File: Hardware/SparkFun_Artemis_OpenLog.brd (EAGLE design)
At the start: 30.5 x 30.5 mm, 112 parts, among them J11 Qwiic, J14 CORTEX_JTAG, J17 MICRO-SD, Q1 20V/0.2A/8MHz/1.2Ω/1Vth, Q10 20V/0.2A/8MHz/1.2Ω/1Vth, Q3 20V/0.2A/8MHz/1.2Ω/1Vth, Q7 20V/0.2A/8MHz/1.2Ω/1Vth, Q9 20V/0.2A/8MHz/1.2Ω/1Vth, U10 CH340E, U13 ICM-20948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

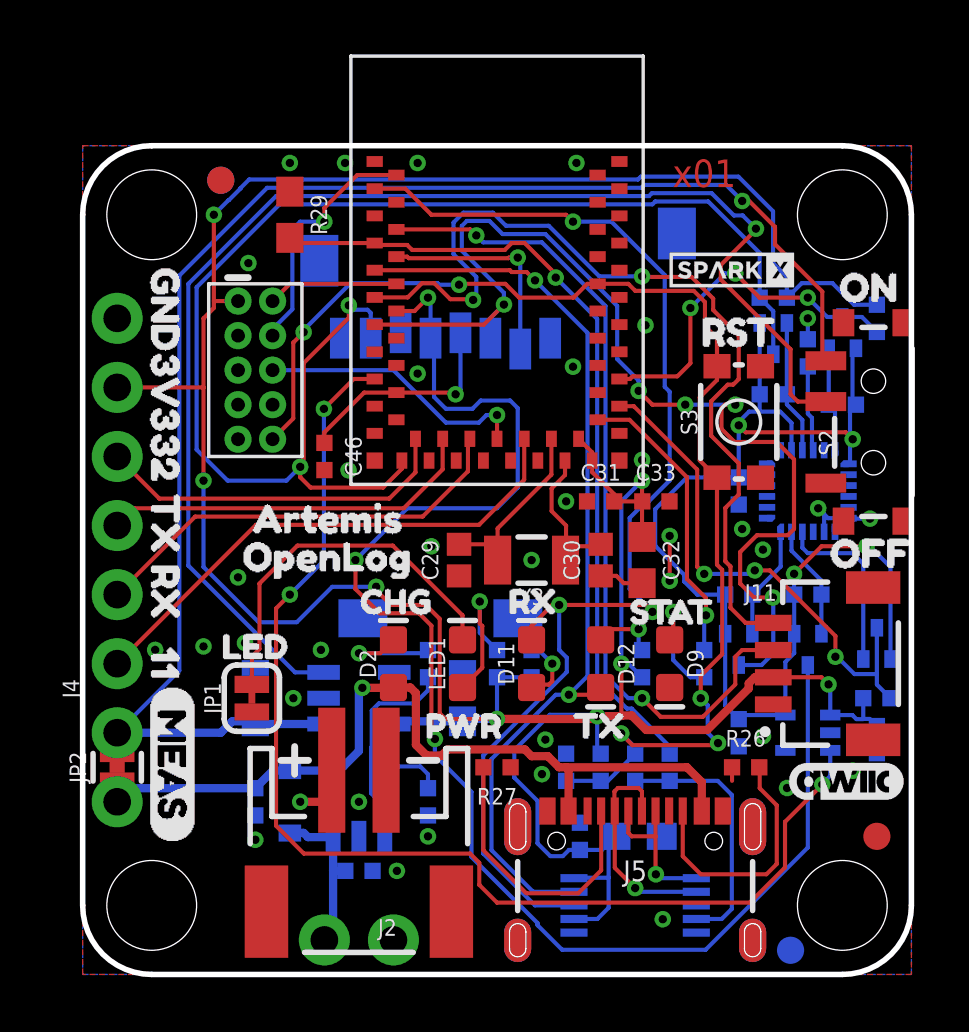
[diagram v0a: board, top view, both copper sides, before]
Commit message: Add RTC cap. Remove switch. Add Qwiic MOSFET.
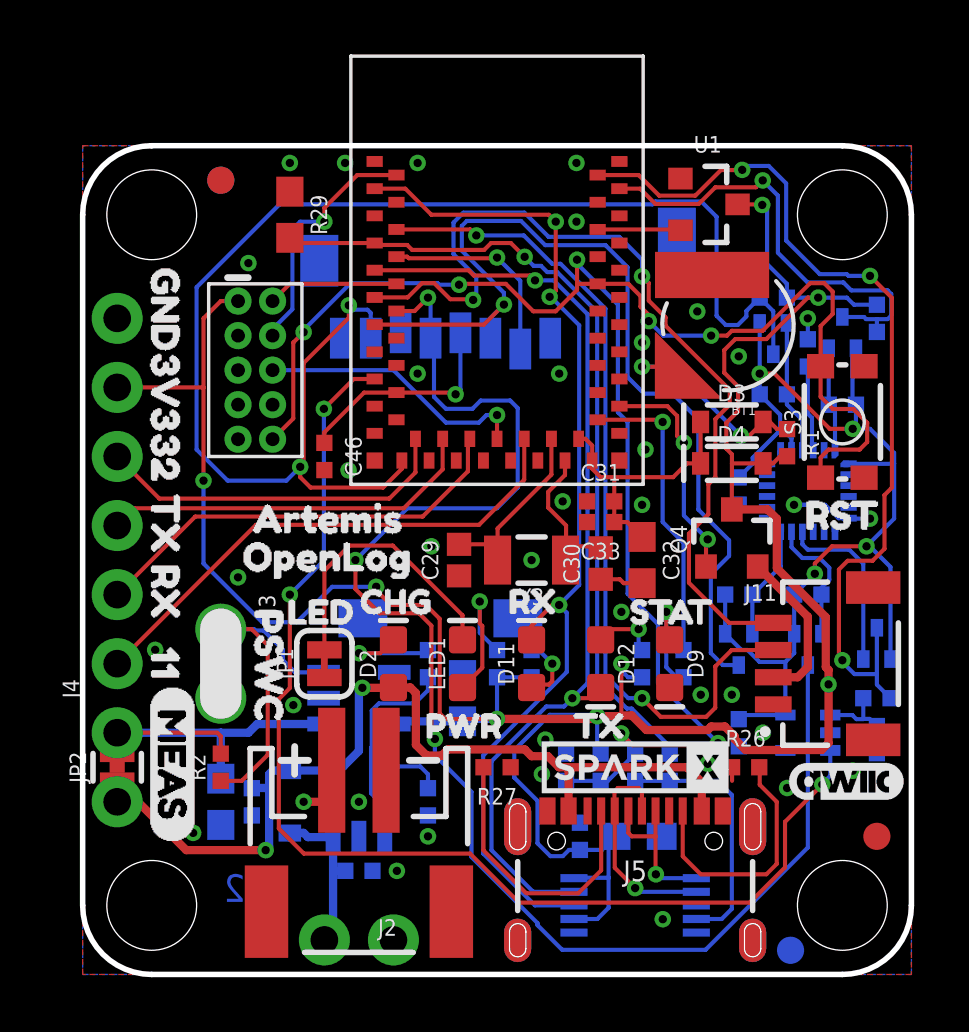
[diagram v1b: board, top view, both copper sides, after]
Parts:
- removed S2: (no value), SparkFun-Switches:SWITCH_SPST_SMD_A
- removed U$17: (no value), buzzard_labels (13):OFF11
- removed U$19: (no value), buzzard_labels (13):ON10
- added BT1: ML414H_IV01E_BATTERY, SparkFun-Batteries:ML414H_IV01E
- added D3, D4: 3A/10V/280mV, SparkFun-DiscreteSemi:SOD-323
- added J3: (no value), SparkFun-Connectors:1X02_NO_SILK
- added Q4: 20V/4.2A/52mΩ/1.4W, SparkFun-DiscreteSemi:SOT23-3
- added R1: 1k, SparkFun-Resistors:0402-TIGHT
- added R2: 10k, SparkFun-Resistors:0402-TIGHT
- added U$10, U$11: (no value), buzzard_labels:PSWC0
- added U1: 3.2V Supervisor, SparkFun-IC-Power:SOT23-3
- J11: value Qwiic -> QWIIC_RIGHT_ANGLE
- U$6: value SPARKX-LOGO2 -> SPARKX-LOGO3; device SparkX:SPARKX-TINY -> SparkX:SPARKX-SMALL
- moved U$6 18.6 mm to (20.3, 7.62)
- moved U$32 7.73 mm to (25.7, 16.9)
- moved C1 4.02 mm to (5.08, 6.35), turned to 270 degrees
- moved S3 3.81 mm to (27.9, 20.3)
- moved JP1 2.95 mm to (8.89, 11.4)
- moved U$8 2.73 mm to (6.73, 13.3)
- moved C33 2.17 mm to (19.1, 16.6), turned to 180 degrees
- moved R23 0.76 mm to (22.1, 11.4)
- moved C30 0.13 mm to (19.1, 15.1)
- moved C3 0.13 mm to (6.22, 6.35)
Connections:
- new net !POWER_LOSS!: U1.2, U8.D3
- new net N$1: BT1.+, D3.A, R1.1
- new net QWIIC_PWR: Q4.1, U8.~D18
- new net VCC_1: C31.2, C32.1, C33.1, D3.C, D4.C, U8.VDD@36, U8.VDD@37
- new net VREG_EN: J3.1, R2.1, U3.3
- net 3.3V: now also D4.A, Q4.3, R1.2, U1.3; no longer C31.2, C32.1, C33.1, J11.2, U8.VDD@36, U8.VDD@37
- net GND: now also BT1.-, J3.2, U1.1; no longer S2.3
- net ICM_!CS!: now also U8.~D44; no longer U8.~D18
- net ICM_INT: now also U8.~D37; no longer U8.D17
- net N$5: now also J11.2, Q4.2; no longer S2.2, U3.3
- net VIN: now also R2.2; no longer S2.1
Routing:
- net N$5: track 48.9 -> 5.89 mm, vias 1 -> 0
- net VIN: track 56.0 -> 14.7 mm, vias 1 -> 0
- net ARTEMIS_!RESET: track 46.0 -> 65.8 mm, vias 5 -> 7
- net ICM_!CS!: track 19.0 -> 33.9 mm
- net 3.3V: track 120.0 -> 106.1 mm
- net VREG_EN: track 0.00 -> 12.8 mm
- net VCC_1: track 0.00 -> 10.2 mm
- net QWIIC_PWR: track 0.00 -> 8.30 mm, vias 0 -> 2
- net N$1: track 0.00 -> 8.15 mm, vias 0 -> 2
- net ARTEMIS_RX0: track 45.5 -> 38.6 mm
- net MOSI: track 39.8 -> 34.8 mm, vias 5 -> 1
- net ICM-20948-LV_#_1.8V: track 45.4 -> 41.0 mm
- net 5V: track 30.7 -> 34.4 mm, vias 1 -> 2
- net ICM_INT: track 13.2 -> 16.7 mm, vias 3 -> 1
- net N$4: track 13.8 -> 10.3 mm
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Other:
- board text added: "x02"
- board text removed: "x01"

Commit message: Change RTC battery charging circuit. Fix PNP Qwiic MOSFET.
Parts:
- removed D4: 3A/10V/280mV, SparkFun-DiscreteSemi:SOD-323
- added C5: 10uF, SparkFun-Capacitors:0603
- added C6: 1.0uF, SparkFun-Capacitors:0402-TIGHT
- added D6: 1A/23V/620mV, SparkFun-DiscreteSemi:SOD-323
- BT1: value ML414H_IV01E_BATTERY -> ML414H
- C29, C30: device SparkFun-Capacitors:0402 -> SparkFun-Capacitors:0402-TIGHT
- FRAME1: value FRAME-LETTER -> FRAME-LEDGER
- J11: value QWIIC_RIGHT_ANGLE -> (none)
- moved FRAME1 31.8 mm to (19.1, -26.7), flipped to the top
- moved U$1 8.76 mm to (27.9, 15.9)
- moved U$32 6.99 mm to (25.7, 23.9)
- moved R1 0.25 mm to (25.9, 19.8)
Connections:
- net 3.3V: now also C5.1, C6.1, D6.A, Q4.2; no longer D4.A, Q4.3, R1.2, R28.2
- net GND: now also C5.2, C6.2
- net N$5: now also Q4.3; no longer Q4.2
- net VCC_1: now also D6.C, R1.2, R28.2; no longer D4.C
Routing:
- net VCC_1: track 10.2 -> 26.6 mm, vias 0 -> 1
- net N$5: track 5.89 -> 9.18 mm
- net GND: track 6.76 -> 5.17 mm
- net 3.3V: track 106.1 -> 107.1 mm
- net MOSI: track 34.8 -> 35.5 mm
- net SCL: track 32.7 -> 32.0 mm
- net N$20: track 7.34 -> 6.75 mm
- net SDA: track 31.1 -> 31.6 mm
- net N$1: track 8.15 -> 7.62 mm
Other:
- board text added: "x03"
- board text removed: "x02"

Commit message: Update PROD_ID on 3.0V supervisor
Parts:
- U1: value 3.2V Supervisor -> 3.0V Supervisor
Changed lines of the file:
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@@
 <attribute name="VALUE" x="25.346" y="19.812" size="0.6096" layer="27" font="vector" ratio="20" rot="R270" align="top-center"/>
 </element>
-<element name="U1" library="SparkFun-IC-Power" package="SOT23-3" value="3.2V Supervisor" x="22.987" y="28.321" smashed="yes" rot="R270">
+<element name="U1" library="SparkFun-IC-Power" package="SOT23-3" value="3.0V Supervisor" x="22.987" y="28.321" smashed="yes" rot="R270">
 <attribute name="NAME" x="22.987" y="30.226" size="0.6096" layer="25" font="vector" ratio="20" align="bottom-center"/>
-<attribute name="PROD_ID" value="IC-14745" x="22.987" y="28.321" size="1.778" layer="27" font="vector" ratio="15" rot="R270" display="off"/>
+<attribute name="PROD_ID" value="IC-14809" x="22.987" y="28.321" size="1.778" layer="27" font="vector" ratio="15" rot="R270" display="off"/>
 <attribute name="VALUE" x="22.987" y="25.781" size="0.6096" layer="27" font="vector" ratio="20" align="bottom-center"/>
 </element>

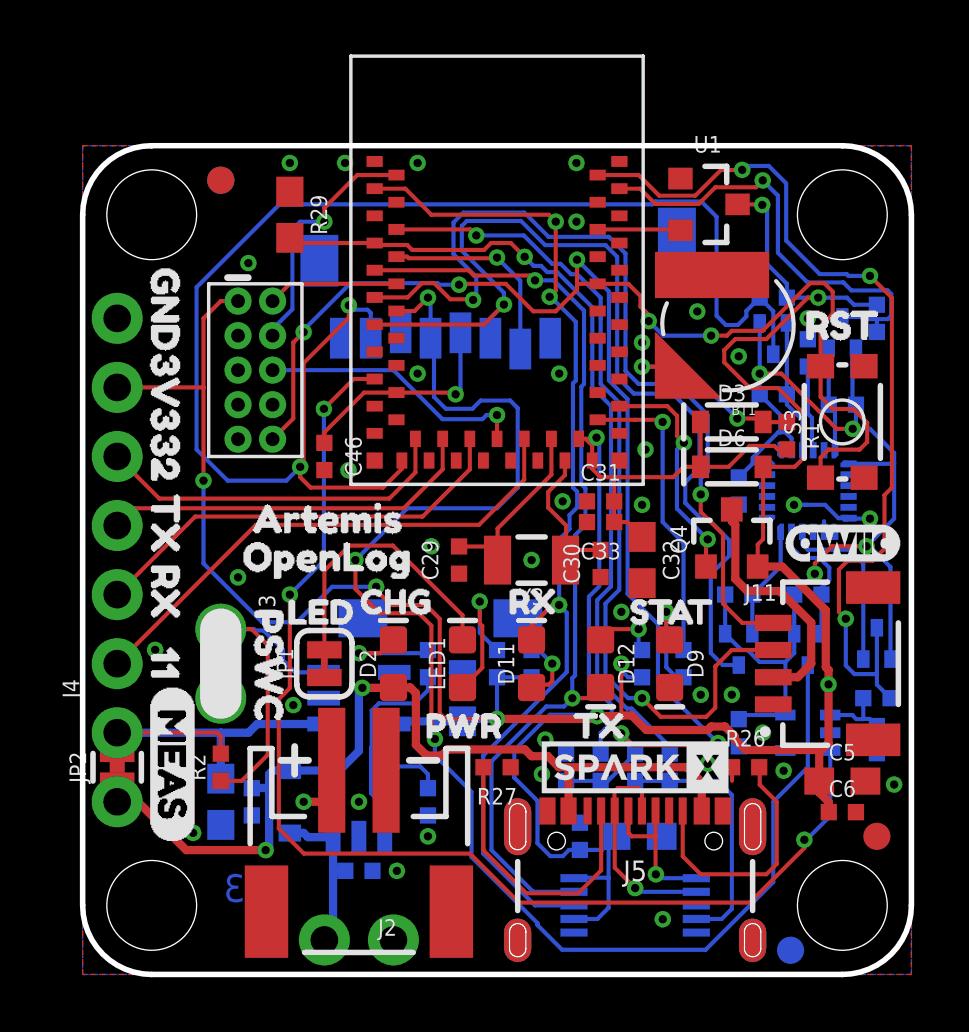
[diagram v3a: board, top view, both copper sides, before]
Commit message: Move SD power to MOSFET control.
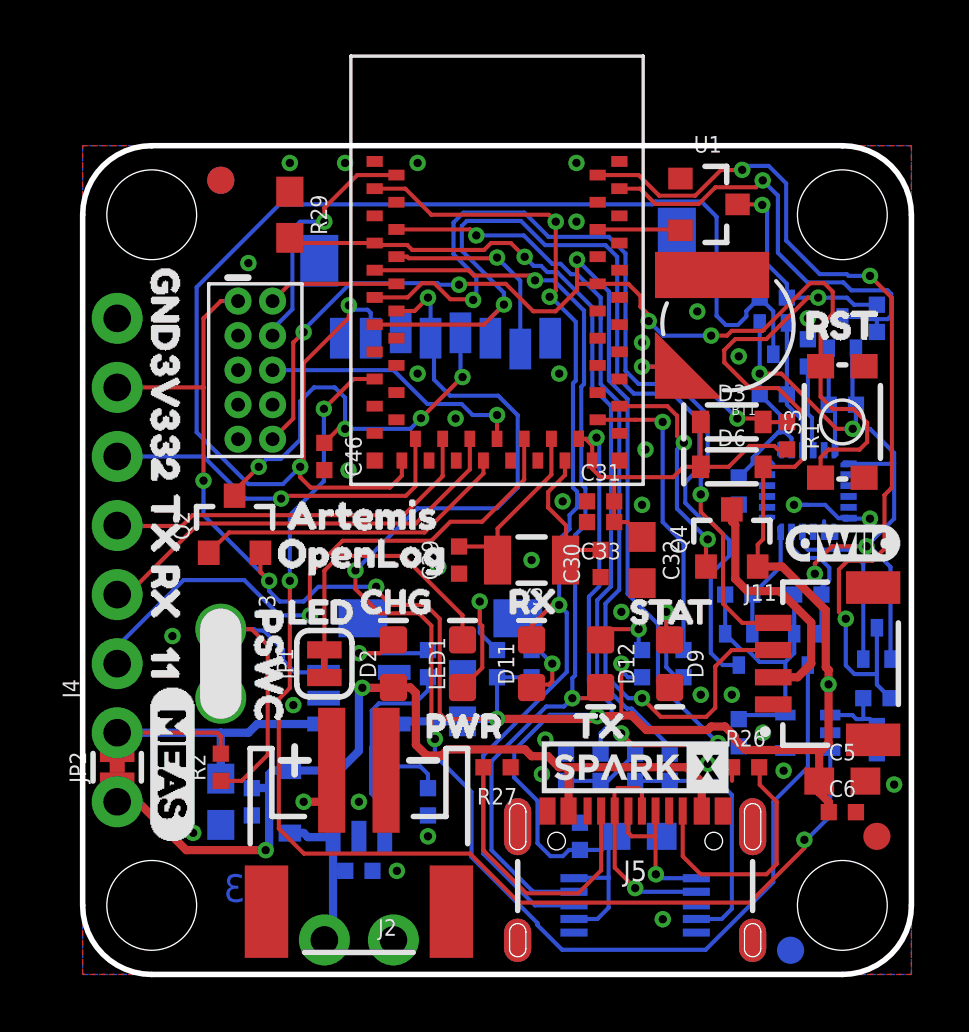
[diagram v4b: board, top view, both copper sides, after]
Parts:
- added Q2: 20V/4.2A/52mΩ/1.4W, SparkFun-DiscreteSemi:SOT23-3
- moved U$9 1.28 mm to (6.60, 16.9)
- moved U$28 1.28 mm to (6.22, 15.5)
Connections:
- new net SD_PWR: C46.1, J17.VCC, Q2.3
- net 3.3V: now also Q2.2
- net MICROSD_PWR: now also Q2.1, U8.D15; no longer C46.1, J17.VCC, U8.~D23
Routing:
- net SD_PWR: track 0.00 -> 15.7 mm, vias 0 -> 4
- net MICROSD_PWR: track 8.18 -> 11.9 mm, vias 1 -> 0
- net ARTEMIS_~AD11: track 19.3 -> 21.6 mm, vias 0 -> 1
- net SCK: track 54.2 -> 53.2 mm
- net ARTEMIS_~AD32: track 13.2 -> 13.5 mm, vias 0 -> 1
- net 3.3V: track 107.1 -> 106.8 mm, vias 8 -> 9
